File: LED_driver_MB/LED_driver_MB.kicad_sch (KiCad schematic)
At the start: 44 parts, among them IC1 MP2393GTL-Z, J1 Conn_01x03_Socket, J2 Conn_01x03_Socket, J3 Conn_01x03_Socket, J4 Conn_01x02_Socket, J5 Conn_01x03_Socket, J6 Conn_01x06, SW1 SW_SPDT, SW2 SW_SPST, SW3 SW_SPST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

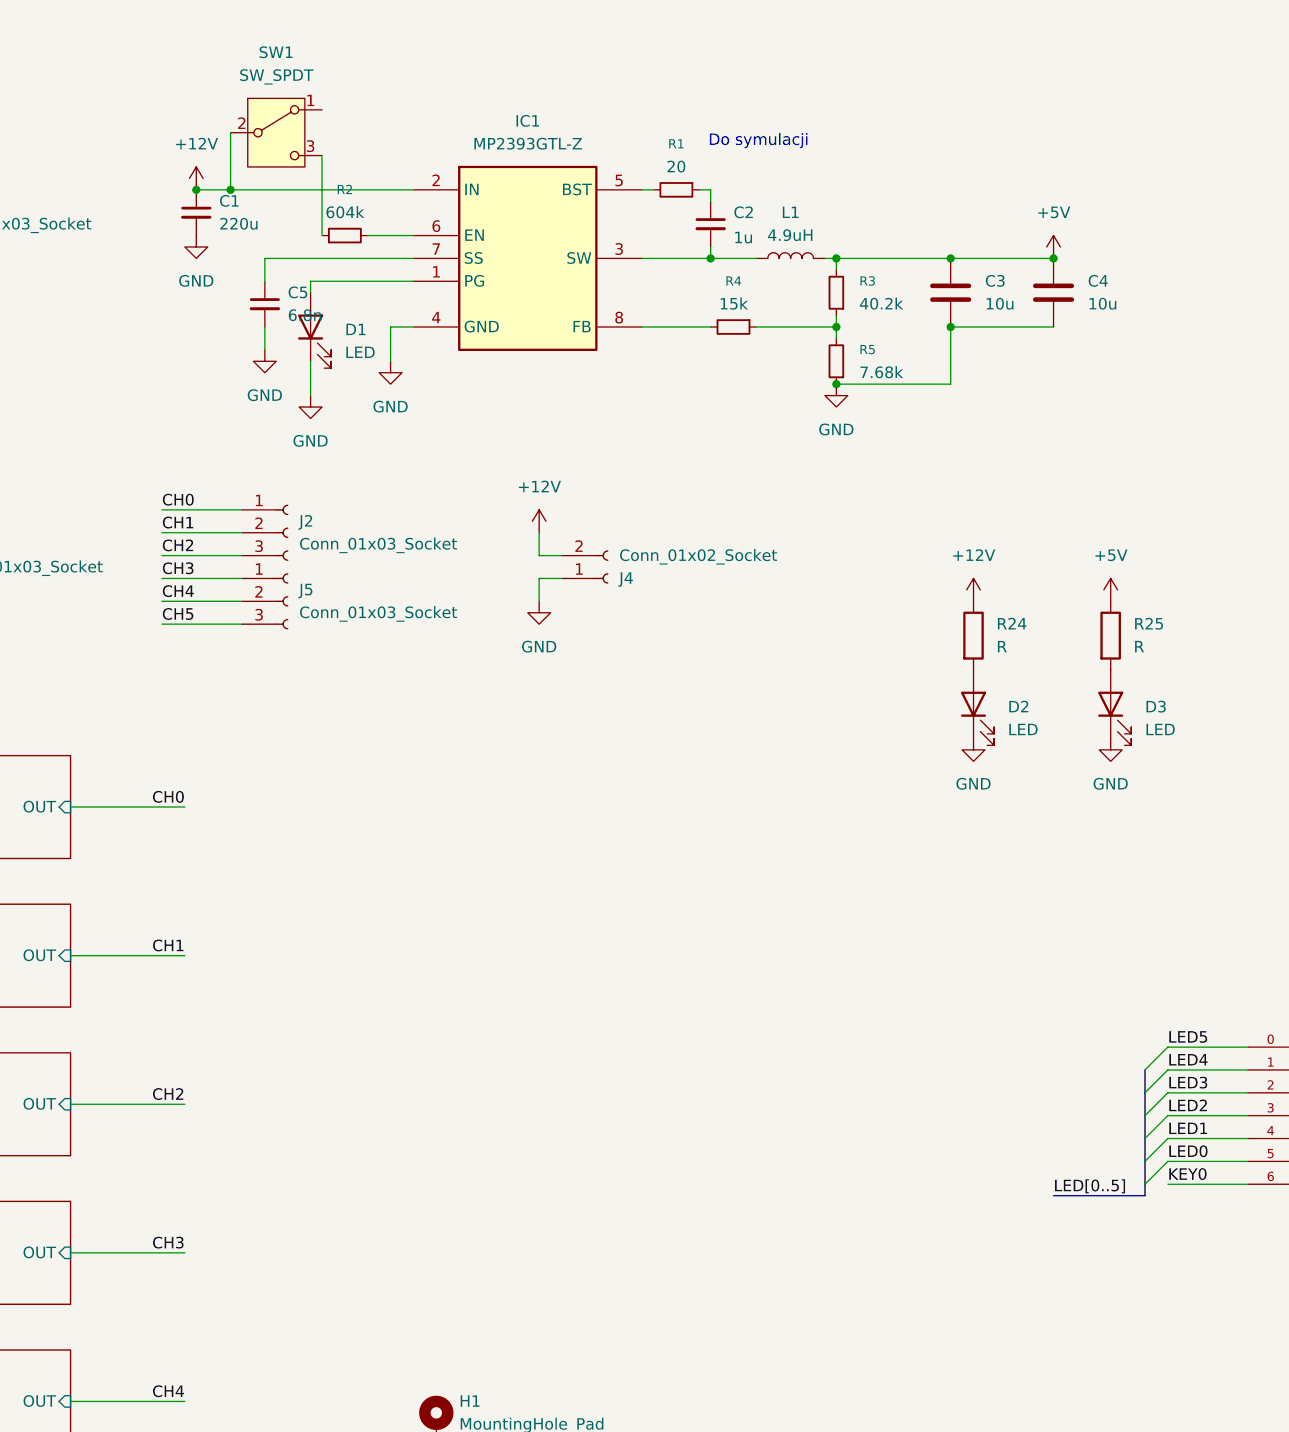
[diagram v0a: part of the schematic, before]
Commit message: change buck converter to TPS563201, production files generated
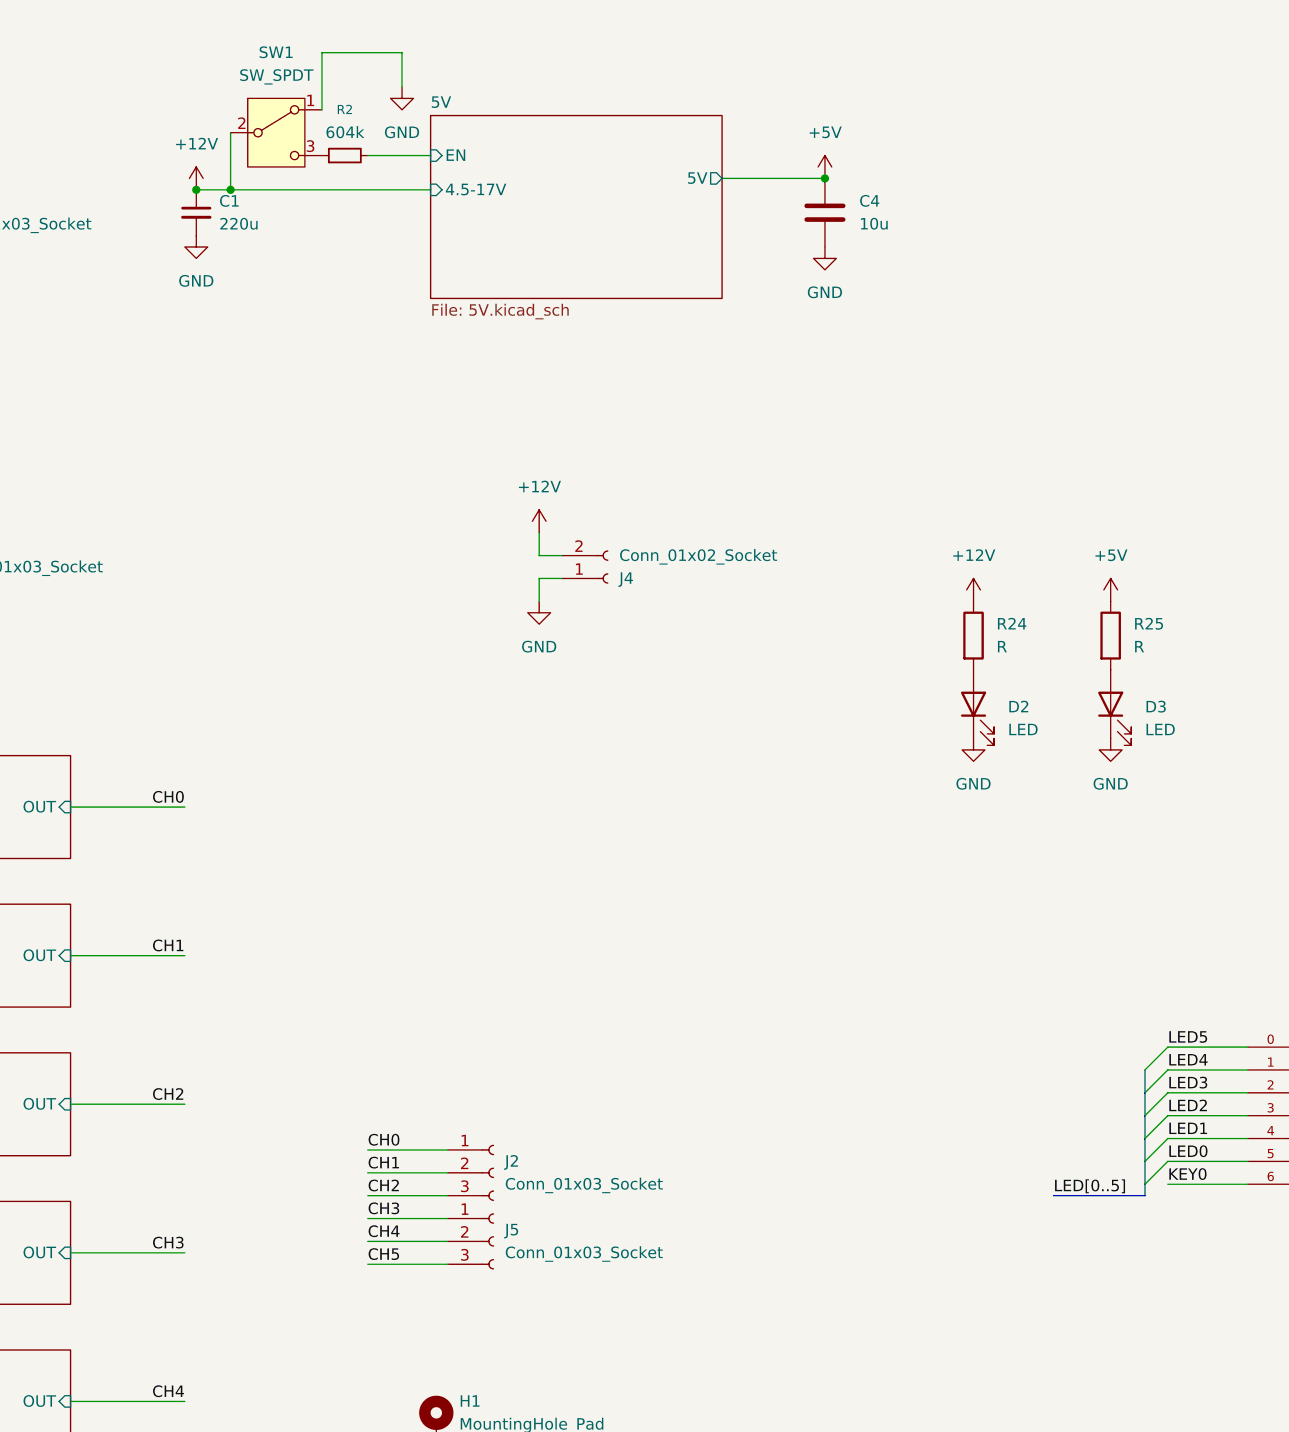
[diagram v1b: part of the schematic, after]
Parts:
- removed C2: 1u, Capacitor_SMD:C_0603_1608Metric, symbol Device:C_Small
- removed C3: 10u, Capacitor_SMD:C_1206_3216Metric, symbol Device:C
- removed C5: 6.8n, Capacitor_SMD:C_0603_1608Metric, symbol Device:C_Small
- removed D1: LED, LED_SMD:LED_0603_1608Metric, symbol Device:LED
- removed IC1: MP2393GTL-Z, SamacSys_Parts:SOTFL50P160X60-8N, symbol SamacSys_Parts:MP2393GTL-Z
- removed L1: 4.9uH, Inductor_SMD:L_10.4x10.4_H4.8, symbol Device:L
- removed R1: 20, Resistor_SMD:R_0603_1608Metric, symbol Device:R_Small
- removed R3: 40.2k, Resistor_SMD:R_0603_1608Metric, symbol Device:R_Small
- removed R4: 15k, Resistor_SMD:R_0603_1608Metric, symbol Device:R_Small
- removed R5: 7.68k, Resistor_SMD:R_0603_1608Metric, symbol Device:R_Small
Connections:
- net GND: now also SW1.1 (A)
- net 5V/EN: now reaches R2.2
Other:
- added sheet 5V (5V.kicad_sch)
- note removed: "Do symulacji"
- moved on the sheet: C4, J2, J5, R2
